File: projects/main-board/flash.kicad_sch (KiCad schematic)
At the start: 10 parts

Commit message: Updated schematics with new symbols
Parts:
- removed U3: ~, symbol symbol-library:MX25UM25645GXDI00
- added U2: MX25UM25645GXDI00, footprint-library:MX25UM25645GXDI00, symbol symbol-library:MX25UM25645GXDI00
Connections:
- net 1V8: now also U2.B4 (VCC), U2.D1 (VCCQ), U2.E4 (VCCQ)
- net CS_N: now also U2.C2 (CS#)
- net DQS: now also U2.C3 (DQS)
- net GND: now also U2.B3 (GND), U2.C1 (VSSQ), U2.E5 (VSSQ)
- net RESET_N: now also U2.A4 (RESET#)
- net SCLK: now also U2.B2 (SCLK)
- net SIO0: now also U2.D3 (SIO0)
- net SIO1: now also U2.D2 (SIO1)
- net SIO2: now also U2.C4 (SIO2)
- net SIO3: now also U2.D4 (SIO3)
- net SIO4: now also U2.D5 (SIO4)
- net SIO5: now also U2.E3 (SIO5)
- net SIO6: now also U2.E2 (SIO6)
- net SIO7: now also U2.E1 (SIO7)
- net at R3.2: now also U2.A5 (ECS#)
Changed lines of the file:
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@@
-	)
-	(symbol
-		(lib_id "symbol-library:MX25UM25645GXDI00")
-		(at 179.07 68.58 0)
-		(unit 1)
-		(exclude_from_sim no)
-		(in_bom yes)
-		(on_board yes)
-		(dnp no)
-		(property "Reference" "U3"
-			(at 180.594 68.072 0)
-			(effects
-				(font
-					(size 1.27 1.27)
-				)
-			)
-		)
-		(property "Value" "~"
-			(at 184.404 68.072 0)
-			(effects
-				(font
-					(size 1.27 1.27)
-				)
-			)
-		)
-		(property "Footprint" ""
-			(at 179.07 68.58 0)
-			(effects
-				(font
-					(size 1.27 1.27)
-				)
-				(hide yes)
-			)
-		)
-		(property "Datasheet" ""
-			(at 179.07 68.58 0)
-			(effects
-				(font
-					(size 1.27 1.27)
-				)
-				(hide yes)
-			)
-		)
-		(property "Description" ""
-			(at 179.07 68.58 0)
-			(effects
-				(font
-					(size 1.27 1.27)
-				)
-				(hide yes)
-			)
-		)
-		(pin "C4"
-		)
-		(pin "D4"
-		)
-		(pin "D5"
-		)
-		(pin "E3"
-		)
-		(pin "E2"
-		)
-		(pin "B2"
-		)
-		(pin "E1"
-		)
-		(pin "A5"
-		)
-		(pin "B1"
-		)
-		(pin "B5"
-		)
-		(pin "C2"
-		)
-		(pin "C3"
-		)
-		(pin "D3"
-		)
-		(pin "D2"
-		)
-		(pin "E4"
-		)
-		(pin "A4"
-		)
-		(pin "C5"
-		)
-		(pin "A2"
-		)
-		(pin "A3"
-		)
-		(pin "B3"
-		)
-		(pin "C1"
-		)
-		(pin "E5"
-		)
-		(pin "B4"
-		)
-		(pin "D1"
-		)
-		(instances
-			(project ""
-				(path "/c621b5fd-2ef7-4a67-960d-0ffc72b1245a/9d6b7d90-1b90-495d-8745-003070f7d46f"
-					(reference "U3")
-					(unit 1)
-				)
-			)
-		)
 	)
 	(symbol
@@
 					(unit 1)
 				)
+			)
+		)
+	)
+	(symbol
+		(lib_name "MX25UM25645GXDI00_1")
+		(lib_id "symbol-library:MX25UM25645GXDI00")
+		(at 179.07 68.58 0)
+		(unit 1)
+		(exclude_from_sim no)
+		(in_bom yes)
+		(on_board yes)
+		(dnp no)
+		(property "Reference" "U2"
+			(at 180.086 68.834 0)
+			(effects
+				(font
+					(size 1.27 1.27)
+				)
+			)
+		)
+		(property "Value" "MX25UM25645GXDI00"
+			(at 188.468 128.27 0)
+			(effects
+				(font
+					(size 1.27 1.27)
+				)
+			)
+		)
+		(property "Footprint" "footprint-library:MX25UM25645GXDI00"
+			(at 194.564 130.048 0)
+			(effects
+				(font
+					(size 1.27 1.27)
+				)
+				(hide yes)
+			)
+		)
+		(property "Datasheet" ""
+			(at 179.07 68.58 0)
+			(effects
+				(font
+					(size 1.27 1.27)
+				)
+				(hide yes)
+			)
+		)
+		(property "Description" ""
+			(at 179.07 68.58 0)
+			(effects
+				(font
+					(size 1.27 1.27)
+				)
+				(hide yes)
+			)
+		)
+		(pin "C2"
+		)
+		(pin "B2"
+		)
+		(pin "C3"
+		)
+		(pin "D3"
+		)
+		(pin "D2"
+		)
+		(pin "C4"
+		)
+		(pin "D4"
+		)
+		(pin "D5"
+		)
+		(pin "E3"
+		)
+		(pin "E2"
+		)
+		(pin "E1"
+		)
+		(pin "A5"
+		)
+		(pin "B1"
+		)
+		(pin "B5"
+		)
+		(pin "C5"
+		)
+		(pin "A2"
+		)
+		(pin "A3"
+		)
+		(pin "B3"
+		)
+		(pin "C1"
+		)
+		(pin "E5"
+		)
+		(pin "A4"
+		)
+		(pin "E4"
+		)
+		(pin "D1"
+		)
+		(pin "B4"
+		)
+		(instances
+			(project ""
+				(path "/c621b5fd-2ef7-4a67-960d-0ffc72b1245a/9d6b7d90-1b90-495d-8745-003070f7d46f"
+					(reference "U2")
+					(unit 1)
+				)

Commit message: Re-annotate schematics.
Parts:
- renumbered C54 to C53, C55 to C54, C56 to C55, C53 to C56, R5 to R41, R4 to R42, R3 to R43, U2 to U3
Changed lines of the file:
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@@
 		(dnp no)
 		(fields_autoplaced yes)
-		(property "Reference" "C54"
+		(property "Reference" "C53"
 			(at 76.2 74.9362 0)
 			(effects
@@
 			(project "main-board"
 				(path "/c621b5fd-2ef7-4a67-960d-0ffc72b1245a/9d6b7d90-1b90-495d-8745-003070f7d46f"
-					(reference "C54")
+					(reference "C53")
 					(unit 1)
 				)
@@
 		(dnp no)
 		(fields_autoplaced yes)
-		(property "Reference" "#PWR080"
+		(property "Reference" "#PWR088"
 			(at 200.66 132.08 0)
 			(effects
@@
 			(project "main-board"
 				(path "/c621b5fd-2ef7-4a67-960d-0ffc72b1245a/9d6b7d90-1b90-495d-8745-003070f7d46f"
-					(reference "#PWR080")
+					(reference "#PWR088")
 					(unit 1)
 				)
@@
 		(on_board yes)
 		(dnp no)
-		(property "Reference" "R4"
+		(property "Reference" "R42"
 			(at 167.894 74.93 0)
 			(effects
@@
 			(project "main-board"
 				(path "/c621b5fd-2ef7-4a67-960d-0ffc72b1245a/9d6b7d90-1b90-495d-8745-003070f7d46f"
-					(reference "R4")
+					(reference "R42")
 					(unit 1)
 				)
@@
 		(dnp no)
 		(fields_autoplaced yes)
-		(property "Reference" "C56"
+		(property "Reference" "C55"
 			(at 104.14 74.9362 0)
 			(effects
@@
 			(project "main-board"
 				(path "/c621b5fd-2ef7-4a67-960d-0ffc72b1245a/9d6b7d90-1b90-495d-8745-003070f7d46f"
-					(reference "C56")
+					(reference "C55")
 					(unit 1)
 				)
@@
 		(dnp no)
 		(fields_autoplaced yes)
-		(property "Reference" "C55"
+		(property "Reference" "C54"
 			(at 90.17 74.9362 0)
 			(effects
@@
 			(project "main-board"
 				(path "/c621b5fd-2ef7-4a67-960d-0ffc72b1245a/9d6b7d90-1b90-495d-8745-003070f7d46f"
-					(reference "C55")
+					(reference "C54")
 					(unit 1)
 				)
@@
 		(dnp no)
 		(fields_autoplaced yes)
-		(property "Reference" "C53"
+		(property "Reference" "C56"
 			(at 118.11 74.9362 0)
 			(effects
@@
 			(project "main-board"
 				(path "/c621b5fd-2ef7-4a67-960d-0ffc72b1245a/9d6b7d90-1b90-495d-8745-003070f7d46f"
-					(reference "C53")
+					(reference "C56")
 					(unit 1)
 				)
@@
 		(dnp no)
 		(fields_autoplaced yes)
-		(property "Reference" "#PWR077"
+		(property "Reference" "#PWR085"
 			(at 73.66 74.93 0)
 			(effects
@@
 			(project ""
 				(path "/c621b5fd-2ef7-4a67-960d-0ffc72b1245a/9d6b7d90-1b90-495d-8745-003070f7d46f"
-					(reference "#PWR077")
+					(reference "#PWR085")
 					(unit 1)
 				)
@@
 		(dnp no)
 		(fields_autoplaced yes)
-		(property "Reference" "#PWR078"
+		(property "Reference" "#PWR086"
 			(at 73.66 87.63 0)
 			(effects
@@
 			(project ""
 				(path "/c621b5fd-2ef7-4a67-960d-0ffc72b1245a/9d6b7d90-1b90-495d-8745-003070f7d46f"
-					(reference "#PWR078")
+					(reference "#PWR086")
 					(unit 1)
 				)
@@
 		(on_board yes)
 		(dnp no)
-		(property "Reference" "U2"
+		(property "Reference" "U3"
 			(at 180.086 68.834 0)
 			(effects
@@
 			(project ""
 				(path "/c621b5fd-2ef7-4a67-960d-0ffc72b1245a/9d6b7d90-1b90-495d-8745-003070f7d46f"
-					(reference "U2")
+					(reference "U3")
 					(unit 1)
 				)
@@
 		(dnp no)
 		(fields_autoplaced yes)
-		(property "Reference" "R3"
+		(property "Reference" "R43"
 			(at 203.2 83.8199 0)
 			(effects
@@
 			(project ""
 				(path "/c621b5fd-2ef7-4a67-960d-0ffc72b1245a/9d6b7d90-1b90-495d-8745-003070f7d46f"
-					(reference "R3")
+					(reference "R43")
 					(unit 1)
 				)
@@
 		(on_board yes)
 		(dnp no)
-		(property "Reference" "R5"
+		(property "Reference" "R41"
 			(at 160.274 74.93 0)
 			(effects
@@
 			(project "main-board"
 				(path "/c621b5fd-2ef7-4a67-960d-0ffc72b1245a/9d6b7d90-1b90-495d-8745-003070f7d46f"
-					(reference "R5")
+					(reference "R41")
 					(unit 1)
 				)
@@
 		(dnp no)
 		(fields_autoplaced yes)
-		(property "Reference" "#PWR079"
+		(property "Reference" "#PWR087"
 			(at 200.66 85.09 0)
 			(effects
@@
 			(project "main-board"
 				(path "/c621b5fd-2ef7-4a67-960d-0ffc72b1245a/9d6b7d90-1b90-495d-8745-003070f7d46f"
-					(reference "#PWR079")
-					(unit 1)
-				)
+					(reference "#PWR087")
+					(unit 1)
+				)

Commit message: Add capacitor part library.
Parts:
- C53, C54, C55: value 4.7uF 6.3V -> 4.7uF 10V
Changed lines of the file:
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@@
 			)
 		)
-		(property "Value" "4.7uF 6.3V"
+		(property "Value" "4.7uF 10V"
 			(at 76.2 77.4762 0)
 			(effects
@@
 			)
 		)
-		(property "Value" "4.7uF 6.3V"
+		(property "Value" "4.7uF 10V"
 			(at 104.14 77.4762 0)
 			(effects
@@
 			)
 		)
-		(property "Value" "4.7uF 6.3V"
+		(property "Value" "4.7uF 10V"
 			(at 90.17 77.4762 0)
 			(effects

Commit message: Normalise capacitors
- Add capacitor parts to library.
- Replace all placeholder capacitors
  with the actual part numbers.
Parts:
- removed C53, C54, C55: 4.7uF 10V, symbol Device:C_Small
- removed C56, C57, C58: 100nF 10V, symbol Device:C_Small
- added C53, C54, C55: 4.7uF 10V, Capacitor_SMD:C_0402_1005Metric, symbol symbol-library-capacitors:CC0402MRX5R6BB475
- added C56, C57, C58: 100nF 10V, Capacitor_SMD:C_0402_1005Metric, symbol symbol-library-capacitors:CC0402KRX7R6BB104
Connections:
- net 1V8: now also C53.1, C54.1, C55.1, C56.1, C57.1, C58.1
- net GND: now also C53.2, C54.2, C55.2, C56.2, C57.2, C58.2

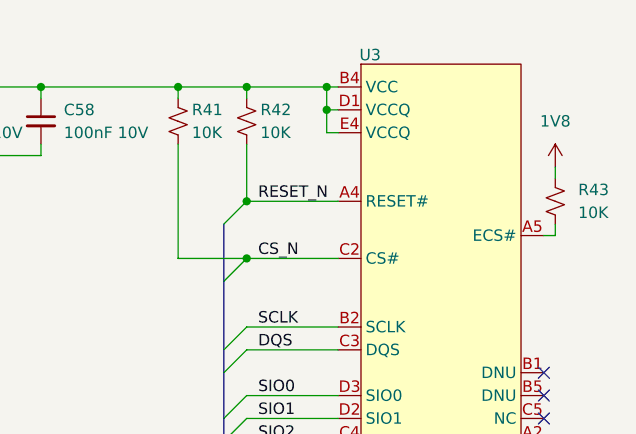
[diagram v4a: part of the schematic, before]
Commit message: Replace placeholder resistors
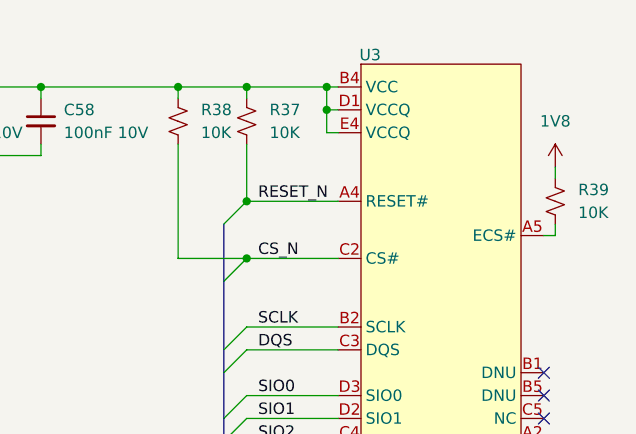
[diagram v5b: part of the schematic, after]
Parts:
- removed R41, R42, R43: 10K, symbol Device:R_Small_US
- added R37, R38, R39: 10K, Resistor_SMD:R_0402_1005Metric, symbol symbol-library-resistors:RC0402JR-0710KL
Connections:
- net 1V8: now also R37.1, R38.1, R39.1
- net CS_N: now also R38.2
- net RESET_N: now also R37.2
- net at U3.A5 (ECS#): now also R39.2

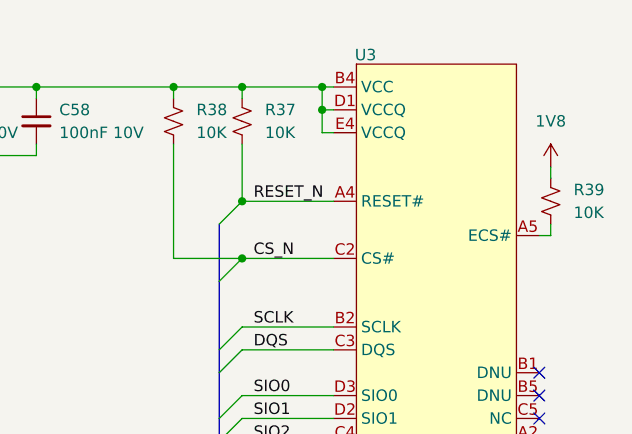
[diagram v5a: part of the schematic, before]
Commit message: Add footprints
- Inductors
- Switches
- Buttons
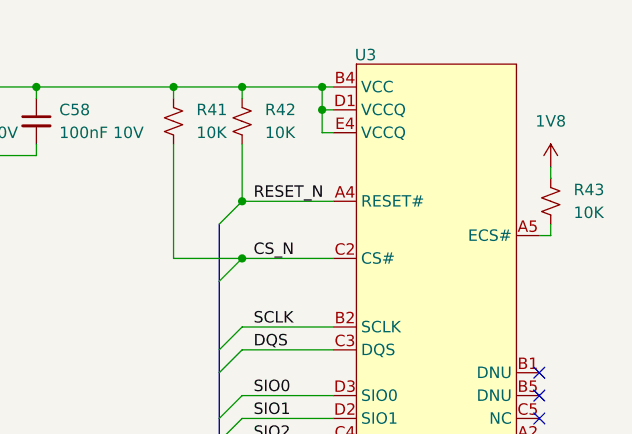
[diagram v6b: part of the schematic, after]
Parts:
- renumbered R38 to R41, R37 to R42, R39 to R43
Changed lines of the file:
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@@
 		(dnp no)
 		(fields_autoplaced yes)
-		(property "Reference" "R37"
+		(property "Reference" "R42"
 			(at 168.91 74.9299 0)
 			(effects
@@
 			(project "main-board"
 				(path "/c621b5fd-2ef7-4a67-960d-0ffc72b1245a/9d6b7d90-1b90-495d-8745-003070f7d46f"
-					(reference "R37")
+					(reference "R42")
 					(unit 1)
 				)
@@
 		(dnp no)
 		(fields_autoplaced yes)
-		(property "Reference" "R38"
+		(property "Reference" "R41"
 			(at 161.29 74.9299 0)
 			(effects
@@
 			(project "main-board"
 				(path "/c621b5fd-2ef7-4a67-960d-0ffc72b1245a/9d6b7d90-1b90-495d-8745-003070f7d46f"
-					(reference "R38")
+					(reference "R41")
 					(unit 1)
 				)
@@
 		(dnp no)
 		(fields_autoplaced yes)
-		(property "Reference" "R39"
+		(property "Reference" "R43"
 			(at 203.2 83.8199 0)
 			(effects
@@
 			(project "main-board"
 				(path "/c621b5fd-2ef7-4a67-960d-0ffc72b1245a/9d6b7d90-1b90-495d-8745-003070f7d46f"
-					(reference "R39")
-					(unit 1)
-				)
+					(reference "R43")
+					(unit 1)
+				)

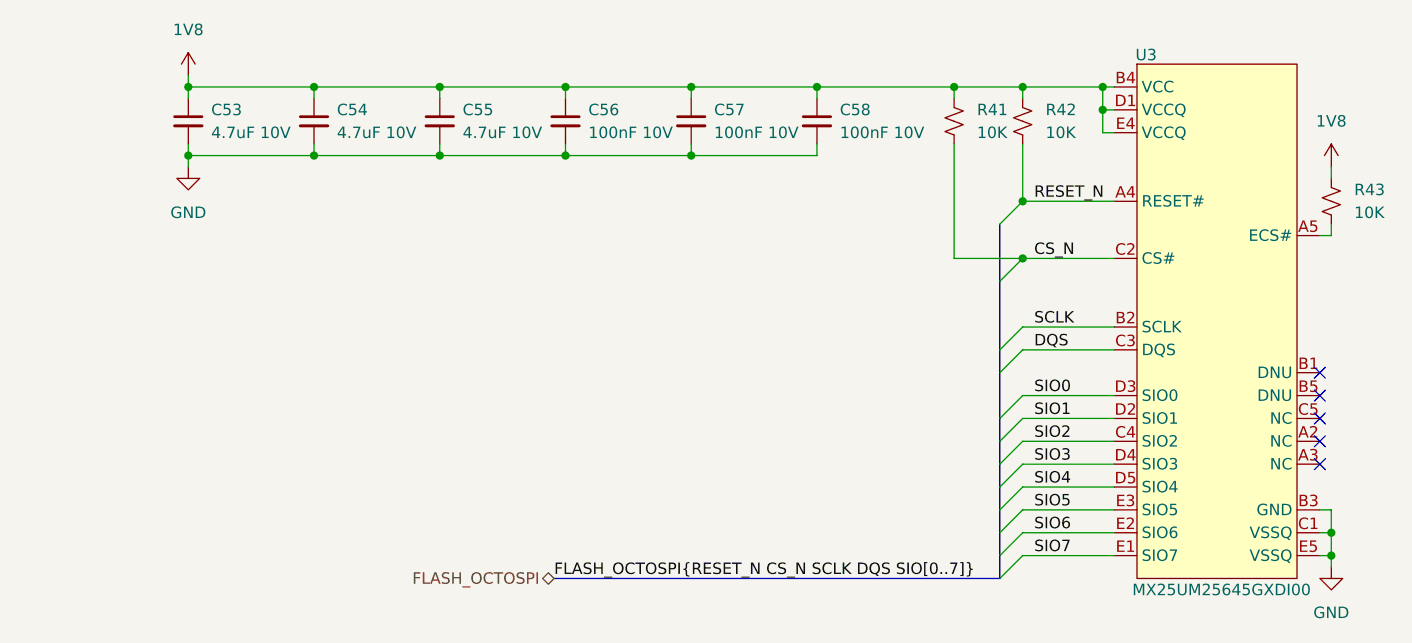
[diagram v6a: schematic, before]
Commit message: Rough PCB component grouping and layout
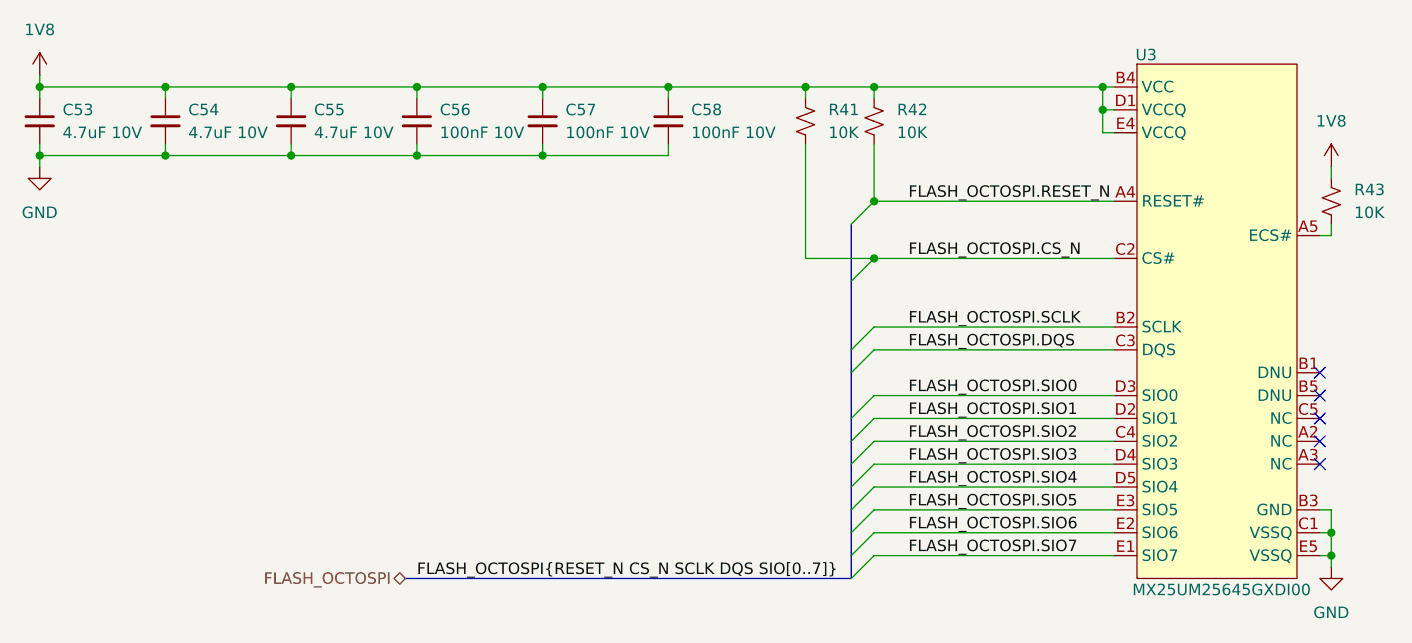
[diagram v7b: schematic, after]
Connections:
- net CS_N renamed FLASH_OCTOSPI.CS_N
- net DQS renamed FLASH_OCTOSPI.DQS
- net RESET_N renamed FLASH_OCTOSPI.RESET_N
- net SCLK renamed FLASH_OCTOSPI.SCLK
- net SIO0 renamed FLASH_OCTOSPI.SIO0
- net SIO1 renamed FLASH_OCTOSPI.SIO1
- net SIO2 renamed FLASH_OCTOSPI.SIO2
- net SIO3 renamed FLASH_OCTOSPI.SIO3
- net SIO4 renamed FLASH_OCTOSPI.SIO4
- net SIO5 renamed FLASH_OCTOSPI.SIO5
- net SIO6 renamed FLASH_OCTOSPI.SIO6
- net SIO7 renamed FLASH_OCTOSPI.SIO7
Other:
- moved on the sheet: C53, C54, C55, C56, C57, C58, R41, R42
